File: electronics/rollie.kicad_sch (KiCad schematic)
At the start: 12 parts, among them J1 Jack-DC, J2 Vcc, J3 Probe, J4 Relay In, J5 Vcc, J6 Serial, J7 Servo PWM, K1 DIPxx-1Cxx-51x, SW1 SW_Push

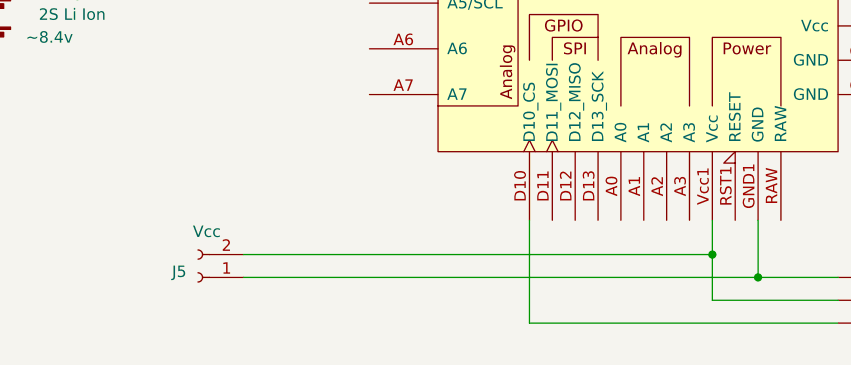
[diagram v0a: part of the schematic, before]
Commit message: Adding ext power probe
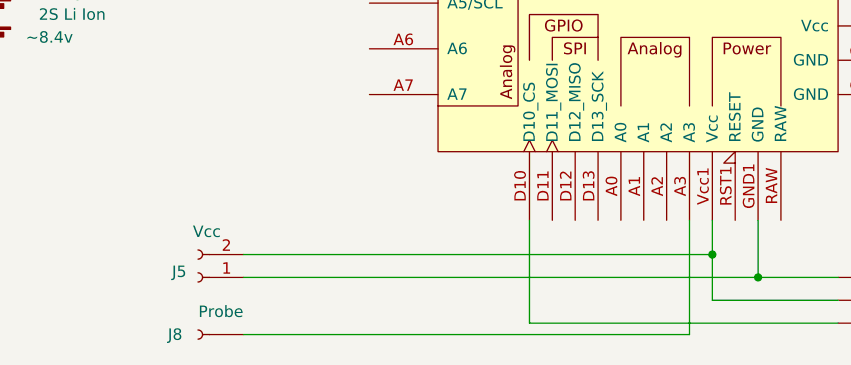
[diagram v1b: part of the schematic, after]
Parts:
- added J8: Probe, symbol Connector:Conn_01x01_Socket
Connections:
- net at XA1.A3: now also J8.1 (Pin_1)
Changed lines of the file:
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@@
+    (stroke (width 0) (type default))
+  )
+  (wire (pts (xy 106.68 83.82) (xy 156.21 83.82))
     (stroke (width 0) (type default))
   )
@@
   )
   (wire (pts (xy 45.72 29.21) (xy 45.72 36.83))
+    (stroke (width 0) (type default))
+  )
+  (wire (pts (xy 156.21 83.82) (xy 156.21 71.12))
     (stroke (width 0) (type default))
   )
@@
         )
       )
+    )
+  )
+  (symbol (lib_id "Connector:Conn_01x01_Socket") (at 101.6 83.82 180) (unit 1)
+    (in_bom yes) (on_board yes) (dnp no)
+    (property "Reference" "J8" (at 99.06 83.82 0)
+      (effects (font (size 1.27 1.27)))
+    )
+    (property "Value" "Probe" (at 104.14 81.28 0)
+      (effects (font (size 1.27 1.27)))
+    )
+    (property "Footprint" "" (at 101.6 83.82 0)
+      (effects (font (size 1.27 1.27)) hide)
+    )
+    (property "Datasheet" "~" (at 101.6 83.82 0)
+      (effects (font (size 1.27 1.27)) hide)
+    )
+    (pin "1")
+    (instances
+      (project "rollie"
+        (path "/21ef0648-144d-4869-9598-e74abff26616"
+          (reference "J8") (unit 1)
+        )
+      )
